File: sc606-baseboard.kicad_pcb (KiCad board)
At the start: 2 copper layers, 100 x 90 mm, 398 parts, among them IC1 TPS54561DPRT, IC2 TPS7A0518PDBVT, J1 PJ-202A, J10 WE_632723300011, J11 WE_632723300011, J12 U_FL-R-SMT-1_10_, J2 WE_68715014522, J3 F52R-1A7H1-11020, J4 46756-1001, J5 U_FL-R-SMT-1_10_, J6 U_FL-R-SMT-1_10_, J7 DM3AT-SF-PEJM5, J8 693022010811, J9 0473460001, M1 SC606T, Q1 BSS138APW, Q2 BSS138-7-F, Q3 BSS138APW, Q4 BSS138APW, Q5 BSS138APW, Q6 BSS138APW, Q7 BSS138-7-F, Q8 BSS138-7-F, SW1 1X03, U1 AP62301WU-7, U10 NCP163ASN330T1G, U11 EMIF06-MSD02N16, U12 FSUSB30MUX, U13 FT232RQ-REEL, U15 USB57442G, U2 AP62301WU-7, U3 AP62301WU-7, U4 74LVC1G123GN, U5 NTS0102GT, U6 PCA9547BS, U7 LT9611UXC, U8 NTS0102GT, U9 TPD13S523PWR, Y1 ABM8G-24.000MHZ-18-D2Y-T, Y2 ABM8G-25.000MHZ-B4Y-T

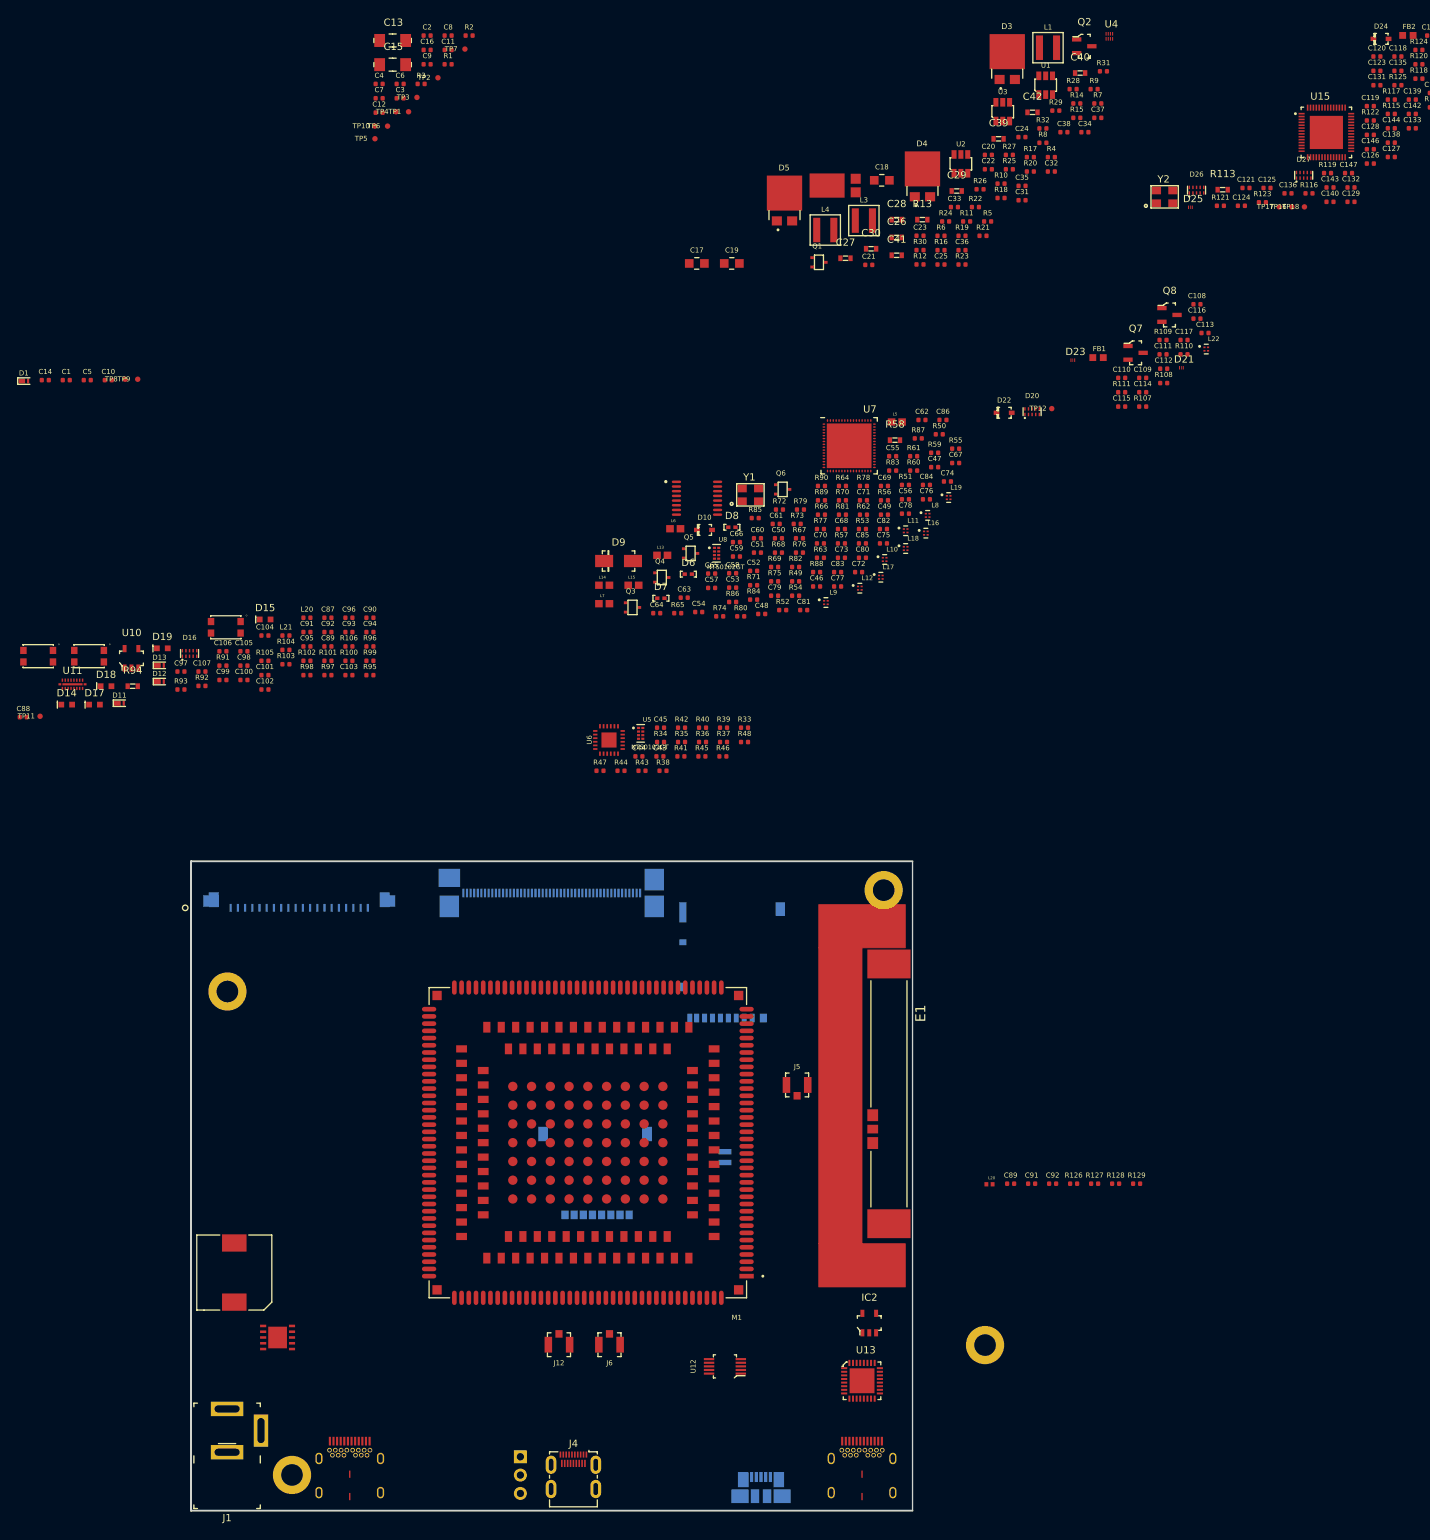
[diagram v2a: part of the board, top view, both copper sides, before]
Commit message: Main components placed on board
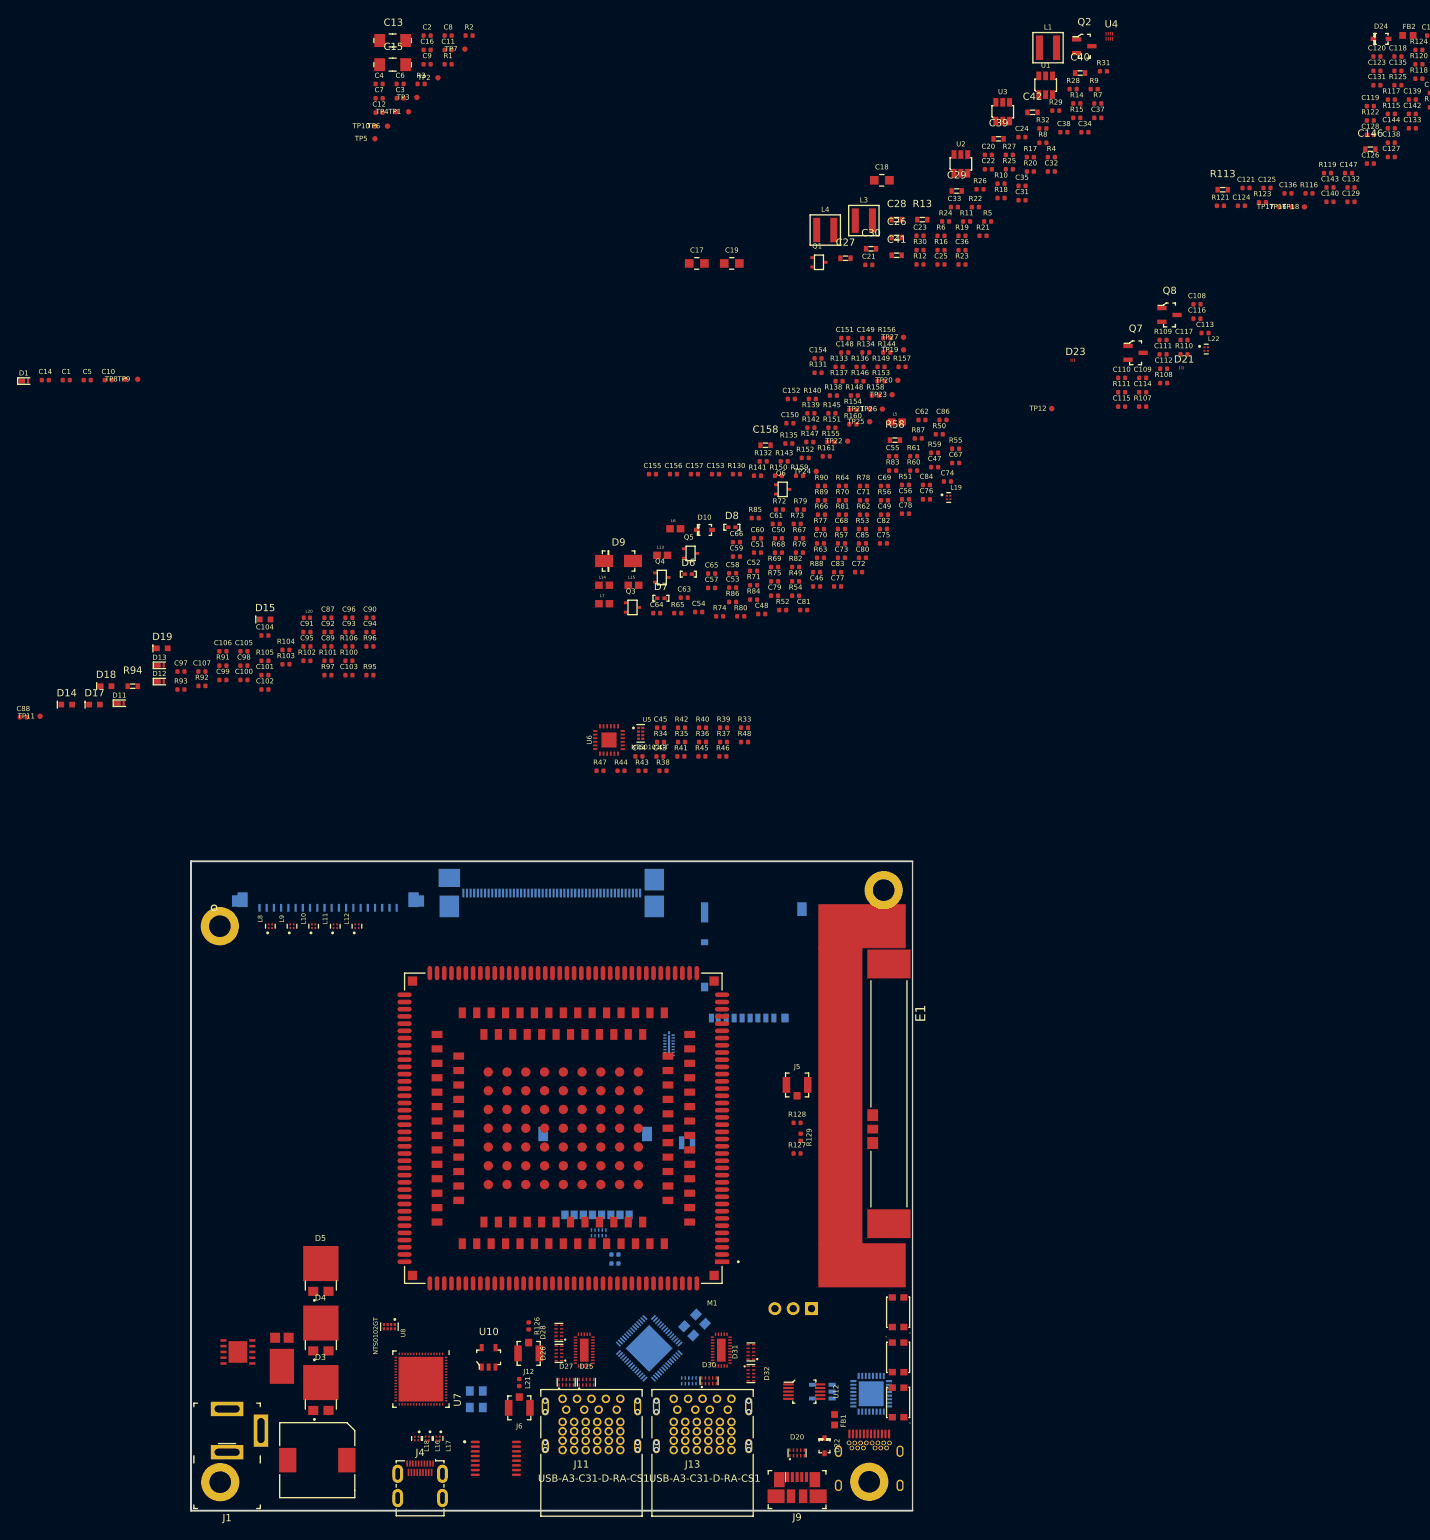
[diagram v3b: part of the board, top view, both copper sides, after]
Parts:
- removed the C89 at (188.6, 84.7)
- removed the C91 at (191.5, 84.7)
- removed the C92 at (194.4, 84.7)
- removed the L20 at (185.7, 84.8)
- added C148: C_100n_0402, sc606-baseboard-footprints:0402-cap, F.Cu at (165.6, -30.5)
- added C149: C_100n_0402, sc606-baseboard-footprints:0402-cap, F.Cu at (168.5, -32.5)
- added C150: C_100n_0402, sc606-baseboard-footprints:0402-cap, F.Cu at (158.0, -20.7)
- added C151: C_100n_0402, sc606-baseboard-footprints:0402-cap, F.Cu at (165.6, -32.5)
- added C152: C_10u_0402, sc606-baseboard-footprints:0402-cap, F.Cu at (158.2, -24.1)
- added C153: C_100n_0402, sc606-baseboard-footprints:0402-cap, F.Cu at (147.7, -13.7)
- added C154: C_100n_0402, sc606-baseboard-footprints:0402-cap, F.Cu at (161.9, -29.7)
- added C155: C_100n_0402, sc606-baseboard-footprints:0402-cap, F.Cu at (139.0, -13.7)
- added C156: C_100n_0402, sc606-baseboard-footprints:0402-cap, F.Cu at (141.9, -13.7)
- added C157: C_100n_0402, sc606-baseboard-footprints:0402-cap, F.Cu at (144.8, -13.7)
- added C158: C_47u_0603, antmicro-footprints:0603-cap, F.Cu at (154.6, -17.7)
- added D28: PUSB3F96X_PASS, sc606-baseboard-footprints:PUSB3F96X, F.Cu at (126.0, 105.3)
- added D29: PUSB3F96X_PASS, sc606-baseboard-footprints:PUSB3F96X, B.Cu at (144.0, 112.0)
- added D30: PUSB3F96X_PASS, sc606-baseboard-footprints:PUSB3F96X, F.Cu at (146.8, 112.0)
- added D31: PUSB3F96X_PASS, sc606-baseboard-footprints:PUSB3F96X, F.Cu at (152.6, 108.0)
- added D32: PUSB3F96X_PASS, sc606-baseboard-footprints:PUSB3F96X, F.Cu at (152.6, 111.0)
- added IC3: HD3SS3220, antmicro-footprints:RNH0030A, F.Cu at (129.5, 107.8)
- added IC4: HD3SS3220, antmicro-footprints:RNH0030A, F.Cu at (148.5, 107.8)
- added J13: USB-A3-C31-D-RA-CS1, antmicro-footprints:USB-A3-C31-D-RA-CS1, F.Cu at (142.4, 116.0)
- added R130: R_200k_0402, antmicro-footprints:0402-res, F.Cu at (150.6, -13.7)
- added R131: R_10k_0402, antmicro-footprints:0402-res, F.Cu at (161.9, -27.7)
- added R132: R_2k_0402, antmicro-footprints:0402-res, F.Cu at (154.3, -15.4)
- added R133: R_0R_0402, antmicro-footprints:0402-res, F.Cu at (164.8, -28.5)
- added R134: R_0R_0402, antmicro-footprints:0402-res, F.Cu at (168.5, -30.5)
- added R135: R_0R_0402, antmicro-footprints:0402-res, F.Cu at (157.9, -17.9)
- added R136: R_0R_0402, antmicro-footprints:0402-res, F.Cu at (167.7, -28.5)
- added R137: R_0R_0402, antmicro-footprints:0402-res, F.Cu at (164.8, -26.5)
- added R138: R_0R_0402, antmicro-footprints:0402-res, F.Cu at (164.0, -24.5)
- added R139: R_2k_0402, antmicro-footprints:0402-res, F.Cu at (160.9, -22.1)
- added R140: R_2k_0402, antmicro-footprints:0402-res, F.Cu at (161.1, -24.1)
- added R141: R_909k_0402, antmicro-footprints:0402-res, F.Cu at (153.5, -13.4)
- added R142: R_200k_0402, antmicro-footprints:0402-res, F.Cu at (160.9, -20.1)
- added R143: R_0R_0402, antmicro-footprints:0402-res, F.Cu at (157.2, -15.4)
- added R144: R_200k_0402, antmicro-footprints:0402-res, F.Cu at (171.4, -30.5)
- added R145: R_10k_0402, antmicro-footprints:0402-res, F.Cu at (163.8, -22.1)
- added R146: R_2k_0402, antmicro-footprints:0402-res, F.Cu at (167.7, -26.5)
- added R147: R_0R_0402, antmicro-footprints:0402-res, F.Cu at (160.8, -18.1)
- added R148: R_0R_0402, antmicro-footprints:0402-res, F.Cu at (166.9, -24.5)
- added R149: R_0R_0402, antmicro-footprints:0402-res, F.Cu at (170.6, -28.5)
- added R150: R_0R_0402, antmicro-footprints:0402-res, F.Cu at (156.4, -13.4)
- added R151: R_0R_0402, antmicro-footprints:0402-res, F.Cu at (163.8, -20.1)
- added R152: R_0R_0402, antmicro-footprints:0402-res, F.Cu at (160.1, -15.9)
- added R153: R_2k_0402, antmicro-footprints:0402-res, F.Cu at (170.6, -26.5)
- added R154: R_2k_0402, antmicro-footprints:0402-res, F.Cu at (166.7, -22.6)
- added R155: R_0R_0402, sc606-baseboard-footprints:0402-res, F.Cu at (163.7, -18.1)
- added R156: R_0R_0402, sc606-baseboard-footprints:0402-res, F.Cu at (171.4, -32.5)
- added R157: R_0R_0402, sc606-baseboard-footprints:0402-res, F.Cu at (173.5, -28.5)
- added R158: R_0R_0402, sc606-baseboard-footprints:0402-res, F.Cu at (169.8, -24.5)
- added R159: R_909k_0402, antmicro-footprints:0402-res, F.Cu at (159.3, -13.4)
- added R160: R_200k_0402, antmicro-footprints:0402-res, F.Cu at (166.7, -20.6)
- added R161: R_0R_0402, antmicro-footprints:0402-res, F.Cu at (163.0, -16.1)
- added TP19: TP_SMD_0_75MM, sc606-baseboard-footprints:Testpoint_smd_0_75mm, F.Cu at (173.8, -30.8)
- added TP20: TP_SMD_0_75MM, sc606-baseboard-footprints:Testpoint_smd_0_75mm, F.Cu at (173.0, -26.6)
- added TP21: TP_SMD_0_75MM, sc606-baseboard-footprints:Testpoint_smd_0_75mm, F.Cu at (169.1, -22.6)
- added TP22: TP_SMD_0_75MM, sc606-baseboard-footprints:Testpoint_smd_0_75mm, F.Cu at (166.0, -18.2)
- added TP23: TP_SMD_0_75MM, sc606-baseboard-footprints:Testpoint_smd_0_75mm, F.Cu at (172.2, -24.6)
- added TP24: TP_SMD_0_75MM, sc606-baseboard-footprints:Testpoint_smd_0_75mm, F.Cu at (161.7, -14.0)
- added TP25: TP_SMD_0_75MM, sc606-baseboard-footprints:Testpoint_smd_0_75mm, F.Cu at (169.1, -20.9)
- added TP26: TP_SMD_0_75MM, sc606-baseboard-footprints:Testpoint_smd_0_75mm, F.Cu at (170.8, -22.6)
- added TP27: TP_SMD_0_75MM, sc606-baseboard-footprints:Testpoint_smd_0_75mm, F.Cu at (173.8, -32.6)
- C102, C103: value C_0p5_0402 -> C_100n_0402
- C139: value C_100n_0402 -> C_10u_0402
- C146: value C_10u_0402 -> C_47u_0603; footprint sc606-baseboard-footprints:0402-cap -> antmicro-footprints:0603-cap
- C89, C91: value C_0p5_0402 -> C_1u_0402
- C92: value C_6p9_0402 -> C_3p_0402
- C94: value C_0p9_0402 -> C_100n_0402
- D16, IC2, R98, R99, U11, U13, U15, Y1, Y2: moved to B.Cu
- D25: value PESD5V0C2BDFZ -> PUSB3F96X_PASS; footprint sc606-baseboard-footprints:DFN0603-3 -> sc606-baseboard-footprints:PUSB3F96X
- J11: value WE_632723300011 -> USB-A3-C31-D-RA-CS1; footprint sc606-baseboard-footprints:WE_632723300011 -> antmicro-footprints:USB-A3-C31-D-RA-CS1
- J9: moved to F.Cu
- L20: value LQW15AN2N4B00D -> HK10056N8S-T; footprint sc606-baseboard-footprints:0402-res -> sc606-baseboard-footprints:INDC1005X55N
- moved D3 207.5 mm to (93.0, 113.2)
- moved D27 196.0 mm to (127.0, 112.2)
- moved U15 192.9 mm to (138.5, 107.5), turned to 135 degrees
- moved D26 183.8 mm to (126.0, 108.2), turned to 90 degrees
- moved D25 183.1 mm to (129.8, 112.2)
- moved D4 180.4 mm to (93.0, 105.0)
- moved D2 180.1 mm to (87.5, 109.5), turned to 90 degrees
- moved Y2 169.3 mm to (144.8, 104.2), turned to 225 degrees
- moved D5 161.7 mm to (93.0, 96.8)
- moved S1 153.8 mm to (173.0, 108.8), turned to 90 degrees
- moved FB1 151.7 mm to (164.2, 117.4), turned to 270 degrees
- moved D20 147.9 mm to (159.0, 122.0)
- moved D22 145.3 mm to (162.8, 121.0), turned to 270 degrees
- moved S3 144.4 mm to (173.0, 102.5), turned to 270 degrees
- moved L16 143.2 mm to (107.8, 120.0), turned to 270 degrees
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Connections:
- C102 pad 1: Net-(ANT2-Pad7) -> Net-(C102-Pad1)
- C102 pad 2: GND -> /USB_HUB_Connectors/USB_C1_SS_TX2_N
- C103 pad 1: Net-(ANT2-Pad6) -> GND
- C103 pad 2: GND -> /USB_HUB_Connectors/5V0_USB
- C138 pad 2: /USB_HUB_Connectors/USBSS_TX1_P -> /USB_HUB_Connectors/USB_C1_SS_TX1_P
- C139 pad 1: Net-(C139-Pad1) -> /USB_HUB_Connectors/5V0_USB
- C139 pad 2: /USB_HUB_Connectors/USBSS_RX2_N -> GND
- C140 pad 2: /USB_HUB_Connectors/USBSS_RX2_P -> /USB_HUB_Connectors/USB_C1_SS_RX2_N
- C141 pad 2: /USB_HUB_Connectors/USBSS_TX1_N -> /USB_HUB_Connectors/USB_C1_SS_TX1_N
- C142 pad 1: /USB_HUB_Connectors/USBSS_RX1_P -> Net-(C142-Pad1)
- C142 pad 2: Net-(C142-Pad2) -> /USB_HUB_Connectors/USB_C1_SS_RX1_N
- C143 pad 1: /USB_HUB_Connectors/USBSS_TX2_N -> Net-(C143-Pad1)
- C143 pad 2: Net-(C143-Pad2) -> /USB_HUB_Connectors/USB_C1_SS_RX2_P
- C144 pad 1: GND -> Net-(C144-Pad1)
- C144 pad 2: /USB_HUB_Connectors/5V0_USB -> /USB_HUB_Connectors/USB_C1_SS_RX1_P
- C145 pad 1: /USB_HUB_Connectors/USBSS_RX1_N -> GND
- C145 pad 2: Net-(C145-Pad2) -> 3V3_SYS
- C146 pad 1: /USB_HUB_Connectors/5V0_USB -> 5V0_SYS
- C147 pad 1: /USB_HUB_Connectors/USBSS_TX2_P -> Net-(C147-Pad1)
- C147 pad 2: Net-(C147-Pad2) -> /USB_HUB_Connectors/USB_C2_SS_TX1_P
- C89 pad 1: ANT_MAIN -> ANT-WIFI
- C92 pad 1: Net-(ANT2-Pad4) -> Net-(C92-Pad1)
- C92 pad 2: Net-(C91-Pad1) -> ANT_MAIN
- C94 pad 1: Net-(ANT2-Pad4) -> Net-(C94-Pad1)
- C94 pad 2: GND -> /USB_HUB_Connectors/USB_C1_SS_TX2_P
- D25 pad 1: /USB_HUB_Connectors/USB_D_P -> /USB_HUB_Connectors/USB_A1_SS_TX_P
- D25 pad 2: /USB_HUB_Connectors/USB_D_N -> /USB_HUB_Connectors/USB_A1_SS_TX_N
- D26 pad 1: /USB_HUB_Connectors/USBSS_TX2_P -> /USB_HUB_Connectors/USB_C1_D_P
- D26 pad 10: /USB_HUB_Connectors/USBSS_TX2_P -> /USB_HUB_Connectors/USB_C1_D_P
- D26 pad 2: /USB_HUB_Connectors/USBSS_TX2_N -> /USB_HUB_Connectors/USB_C1_D_N
- D26 pad 4: /USB_HUB_Connectors/USBSS_RX2_N -> /USB_HUB_Connectors/USB_A1_D_N
- D26 pad 5: /USB_HUB_Connectors/USBSS_RX2_P -> /USB_HUB_Connectors/USB_A1_D_P
- D26 pad 6: /USB_HUB_Connectors/USBSS_RX2_P -> /USB_HUB_Connectors/USB_A1_D_P
- D26 pad 7: /USB_HUB_Connectors/USBSS_RX2_N -> /USB_HUB_Connectors/USB_A1_D_N
- D26 pad 9: /USB_HUB_Connectors/USBSS_TX2_N -> /USB_HUB_Connectors/USB_C1_D_N
- D27 pad 1: /USB_HUB_Connectors/USBSS_TX1_P -> /USB_HUB_Connectors/USB_C1_SS_RX2_P
- D27 pad 10: /USB_HUB_Connectors/USBSS_TX1_P -> /USB_HUB_Connectors/USB_C1_SS_RX2_P
- D27 pad 2: /USB_HUB_Connectors/USBSS_TX1_N -> /USB_HUB_Connectors/USB_C1_SS_RX2_N
- D27 pad 4: /USB_HUB_Connectors/USBSS_RX1_N -> /USB_HUB_Connectors/USB_C1_SS_TX2_P
- D27 pad 5: /USB_HUB_Connectors/USBSS_RX1_P -> /USB_HUB_Connectors/USB_C1_SS_TX2_N
- D27 pad 6: /USB_HUB_Connectors/USBSS_RX1_P -> /USB_HUB_Connectors/USB_C1_SS_TX2_N
- D27 pad 7: /USB_HUB_Connectors/USBSS_RX1_N -> /USB_HUB_Connectors/USB_C1_SS_TX2_P
- D27 pad 9: /USB_HUB_Connectors/USBSS_TX1_N -> /USB_HUB_Connectors/USB_C1_SS_RX2_N
- J11 pad A10: Net-(C139-Pad1) -> Net-(C140-Pad1)
- J11 pad A11: Net-(C140-Pad1) -> Net-(C143-Pad1)
- J11 pad A6: /USB_HUB_Connectors/USB_1_D_P -> /USB_HUB_Connectors/USB_C1_D_P
- J11 pad A7: /USB_HUB_Connectors/USB_1_D_N -> /USB_HUB_Connectors/USB_C1_D_N
- J11 pad B10: Net-(C145-Pad2) -> Net-(C142-Pad1)
- J11 pad B11: Net-(C142-Pad2) -> Net-(C144-Pad1)
- J11 pad B2: Net-(C147-Pad2) -> Net-(C94-Pad1)
- J11 pad B3: Net-(C143-Pad2) -> Net-(C102-Pad1)
- J11 pad B6: /USB_HUB_Connectors/USB_1_D_P -> /USB_HUB_Connectors/USB_C1_D_P
- J11 pad B7: /USB_HUB_Connectors/USB_1_D_N -> /USB_HUB_Connectors/USB_C1_D_N
- J2 pad 1: /cameras module/CSI0_LN3_N -> CAM1_DATA_7
- J2 pad 10: /cameras module/CSI0_CLK_N -> CAM1_DATA_9
- J2 pad 11: /cameras module/CSI0_CLK_P -> CAM1_DATA_8
- J2 pad 19: /cameras module/CSI1_LN3_N -> CAM2_DATA_7
- J2 pad 2: /cameras module/CSI0_LN3_P -> CAM1_DATA_6
- J2 pad 20: /cameras module/CSI1_LN3_P -> CAM2_DATA_6
- J2 pad 21: /cameras module/CSI1_LN2_N -> CAM2_DATA_5
- J2 pad 22: /cameras module/CSI1_LN2_P -> CAM2_DATA_4
- J2 pad 23: /cameras module/CSI1_LN1_N -> CAM2_DATA_3
- J2 pad 24: /cameras module/CSI1_LN1_P -> CAM2_DATA_2
- J2 pad 25: /cameras module/CSI1_LN0_N -> CAM2_DATA_1
- J2 pad 26: /cameras module/CSI1_LN0_P -> CAM2_DATA_0
- J2 pad 28: /cameras module/CSI1_CLK_N -> CAM2_DATA_9
- J2 pad 29: /cameras module/CSI1_CLK_P -> CAM2_DATA_8
- J2 pad 3: /cameras module/CSI0_LN2_N -> CAM1_DATA_5
- J2 pad 4: /cameras module/CSI0_LN2_P -> CAM1_DATA_4
- J2 pad 5: /cameras module/CSI0_LN1_N -> CAM1_DATA_3
- J2 pad 6: /cameras module/CSI0_LN1_P -> CAM1_DATA_2
- J2 pad 7: /cameras module/CSI0_LN0_N -> CAM1_DATA_1
- J2 pad 8: /cameras module/CSI0_LN0_P -> CAM1_DATA_0
- J7 pad 10: /peripherals/SD_DET -> SD_DATA_6
- L10 pad 1: /display module/DSI0_LN1_N -> SoMtoDisplay_DATA_3
- L10 pad 4: /display module/DSI0_LN1_P -> SoMtoDisplay_DATA_2
- L11 pad 1: /display module/DSI0_LN0_N -> SoMtoDisplay_DATA_1
- L11 pad 4: /display module/DSI0_LN0_P -> SoMtoDisplay_DATA_0
- L12 pad 1: /display module/DSI0_CLK_N -> SoMtoDisplay_DATA_9
- L12 pad 4: /display module/DSI0_CLK_P -> SoMtoDisplay_DATA_8
- L20 pad 1: ANT_MAIN -> Net-(C92-Pad1)
- L20 pad 2: Net-(C91-Pad1) -> GND
- L8 pad 1: /display module/DSI0_LN3_N -> SoMtoDisplay_DATA_7
- L8 pad 4: /display module/DSI0_LN3_P -> SoMtoDisplay_DATA_6
- L9 pad 1: /display module/DSI0_LN2_N -> SoMtoDisplay_DATA_5
- L9 pad 4: /display module/DSI0_LN2_P -> SoMtoDisplay_DATA_4
- M1 pad 102: /SoM/DSI1_CLK_P -> SoMtoDisplay_DATA_8
- M1 pad 103: /SoM/DSI1_CLK_N -> SoMtoDisplay_DATA_9
- M1 pad 104: /SoM/DSI1_LN0_P -> SoMtoDisplay_DATA_0
- M1 pad 105: /SoM/DSI1_LN0_N -> SoMtoDisplay_DATA_1
- M1 pad 106: /SoM/DSI1_LN1_P -> SoMtoDisplay_DATA_2
- M1 pad 107: /SoM/DSI1_LN1_N -> SoMtoDisplay_DATA_3
- M1 pad 108: /SoM/DSI1_LN2_P -> SoMtoDisplay_DATA_4
- M1 pad 109: /SoM/DSI1_LN2_N -> SoMtoDisplay_DATA_5
- M1 pad 110: /SoM/DSI1_LN3_P -> SoMtoDisplay_DATA_6
- M1 pad 111: /SoM/DSI1_LN3_N -> SoMtoDisplay_DATA_7
- M1 pad 115: /SoM/DSI0_CLK_P -> SoMtoHDMI_DATA_8
- M1 pad 116: /SoM/DSI0_CLK_N -> SoMtoHDMI_DATA_9
- M1 pad 117: /SoM/DSI0_LN0_P -> SoMtoHDMI_DATA_0
- M1 pad 118: /SoM/DSI0_LN0_N -> SoMtoHDMI_DATA_1
- M1 pad 119: /SoM/DSI0_LN1_P -> SoMtoHDMI_DATA_2
- M1 pad 120: /SoM/DSI0_LN1_N -> SoMtoHDMI_DATA_3
- M1 pad 121: /SoM/DSI0_LN2_P -> SoMtoHDMI_DATA_4
- M1 pad 122: /SoM/DSI0_LN2_N -> SoMtoHDMI_DATA_5
- M1 pad 123: /SoM/DSI0_LN3_P -> SoMtoHDMI_DATA_6
- M1 pad 124: /SoM/DSI0_LN3_N -> SoMtoHDMI_DATA_7
- M1 pad 183: /SoM/CSI1_CLK_P -> CAM2_DATA_8
- M1 pad 184: /SoM/CSI1_CLK_N -> CAM2_DATA_9
- M1 pad 185: /SoM/CSI1_LN0_P -> CAM2_DATA_0
- M1 pad 186: /SoM/CSI1_LN0_N -> CAM2_DATA_1
- M1 pad 187: /SoM/CSI1_LN1_P -> CAM2_DATA_2
- M1 pad 188: /SoM/CSI1_LN1_N -> CAM2_DATA_3
- M1 pad 189: /SoM/CSI1_LN2_P -> CAM2_DATA_4
- M1 pad 190: /SoM/CSI1_LN2_N -> CAM2_DATA_5
- M1 pad 191: /SoM/CSI1_LN3_P -> CAM2_DATA_6
- M1 pad 192: /SoM/CSI1_LN3_N -> CAM2_DATA_7
- M1 pad 64: /SoM/SD_DET -> SD_DATA_6
- M1 pad 65: /SoM/SD_DATA3 -> SD_DATA_3
- M1 pad 66: /SoM/SD_DATA2 -> SD_DATA_2
- M1 pad 67: /SoM/SD_DATA1 -> SD_DATA_1
- M1 pad 68: /SoM/SD_DATA0 -> SD_DATA_0
- M1 pad 69: /SoM/SD_CMD -> SD_DATA_5
- M1 pad 70: /SoM/SD_CLK -> SD_DATA_4
- M1 pad 88: /SoM/CSI0_CLK_P -> CAM1_DATA_8
- M1 pad 89: /SoM/CSI0_CLK_N -> CAM1_DATA_9
- M1 pad 90: /SoM/CSI0_LN0_P -> CAM1_DATA_0
- M1 pad 91: /SoM/CSI0_LN0_N -> CAM1_DATA_1
- M1 pad 92: /SoM/CSI0_LN1_P -> CAM1_DATA_2
- M1 pad 93: /SoM/CSI0_LN1_N -> CAM1_DATA_3
- M1 pad 94: /SoM/CSI0_LN2_P -> CAM1_DATA_4
- M1 pad 95: /SoM/CSI0_LN2_N -> CAM1_DATA_5
- M1 pad 96: /SoM/CSI0_LN3_P -> CAM1_DATA_6
- M1 pad 97: /SoM/CSI0_LN3_N -> CAM1_DATA_7
- R122 pad 1: /USB_HUB_Connectors/CC2 -> /USB_HUB_Connectors/USB_C1_CC1
- R122 pad 2: Net-(J11-PadA5) -> Net-(J11-PadB5)
- R123 pad 1: /USB_HUB_Connectors/CC1 -> /USB_HUB_Connectors/USB_C1_CC2
- R123 pad 2: Net-(J11-PadA5) -> Net-(J11-PadB5)
- R124 pad 1: /USB_HUB_Connectors/CC2 -> /USB_HUB_Connectors/USB_C1_CC2
- R124 pad 2: Net-(J11-PadB5) -> Net-(J11-PadA5)
- R125 pad 1: /USB_HUB_Connectors/CC1 -> /USB_HUB_Connectors/USB_C1_CC1
- R125 pad 2: Net-(J11-PadB5) -> Net-(J11-PadA5)
- TP18 pad 1: Net-(J11-PadB8) -> Net-(J11-PadA8)
- U11 pad 1: /peripherals/SD_DET -> SD_DATA_6
- U11 pad 3: /peripherals/SD_DATA2 -> SD_DATA_2
- U11 pad 4: /peripherals/SD_DATA3 -> SD_DATA_3
- U11 pad 5: /peripherals/SD_CMD -> SD_DATA_5
- U11 pad 6: /peripherals/SD_CLK -> SD_DATA_4
- U11 pad 7: /peripherals/SD_DATA0 -> SD_DATA_0
- U11 pad 8: /peripherals/SD_DATA1 -> SD_DATA_1
- U15 pad 1: /USB_HUB_Connectors/USB_1_D_P -> /USB_HUB_Connectors/USB_A1_D_P
- U15 pad 10: Net-(U15-Pad10) -> /USB_HUB_Connectors/USB_C1_SS_TX_P
- U15 pad 11: Net-(U15-Pad11) -> /USB_HUB_Connectors/USB_C1_SS_TX_N
- U15 pad 13: Net-(U15-Pad13) -> /USB_HUB_Connectors/USB_C1_SS_RX_P
- U15 pad 14: Net-(U15-Pad14) -> /USB_HUB_Connectors/USB_C1_SS_RX_N
- U15 pad 17: Net-(U15-Pad17) -> /USB_HUB_Connectors/USB_A2_D_P
- U15 pad 18: Net-(U15-Pad18) -> /USB_HUB_Connectors/USB_A2_D_N
- U15 pad 19: Net-(U15-Pad19) -> /USB_HUB_Connectors/USB_A2_SS_TX_P
- U15 pad 2: /USB_HUB_Connectors/USB_1_D_N -> /USB_HUB_Connectors/USB_A1_D_N
- U15 pad 20: Net-(U15-Pad20) -> /USB_HUB_Connectors/USB_A2_SS_TX_N
- U15 pad 22: Net-(U15-Pad22) -> /USB_HUB_Connectors/USB_A2_SS_RX_P
- U15 pad 23: Net-(U15-Pad23) -> /USB_HUB_Connectors/USB_A2_SS_RX_N
- U15 pad 24: Net-(U15-Pad24) -> /USB_HUB_Connectors/USB_C2_D_P
- U15 pad 25: Net-(U15-Pad25) -> /USB_HUB_Connectors/USB_C2_D_N
- U15 pad 26: Net-(U15-Pad26) -> /USB_HUB_Connectors/USB_C2_SS_TX_P
- U15 pad 27: Net-(U15-Pad27) -> /USB_HUB_Connectors/USB_C2_SS_TX_N
- U15 pad 29: Net-(U15-Pad29) -> /USB_HUB_Connectors/USB_C2_SS_RX_P
- U15 pad 3: /USB_HUB_Connectors/USBSS_TX1_P -> /USB_HUB_Connectors/USB_A1_SS_TX_P
- U15 pad 30: Net-(U15-Pad30) -> /USB_HUB_Connectors/USB_C2_SS_RX_N
- U15 pad 4: /USB_HUB_Connectors/USBSS_TX1_N -> /USB_HUB_Connectors/USB_A1_SS_TX_N
- U15 pad 47: SoM_USB3_TX_P -> SoM_USB3_RX_P
- U15 pad 48: SoM_USB3_TX_N -> SoM_USB3_RX_N
- U15 pad 50: SoM_USB3_RX_P -> SoM_USB3_TX_P
- U15 pad 51: SoM_USB3_RX_N -> SoM_USB3_TX_N
- U15 pad 6: /USB_HUB_Connectors/USBSS_RX1_P -> /USB_HUB_Connectors/USB_A1_SS_RX_P
- U15 pad 7: /USB_HUB_Connectors/USBSS_RX1_N -> /USB_HUB_Connectors/USB_A1_SS_RX_N
- U15 pad 8: Net-(U15-Pad8) -> /USB_HUB_Connectors/USB_C1_D_P
- U15 pad 9: Net-(U15-Pad9) -> /USB_HUB_Connectors/USB_C1_D_N
- U7 pad 10: /display module/DSI1_CLK_P -> SoMtoHDMI_DATA_8
- U7 pad 11: /display module/DSI1_LN1_N -> SoMtoHDMI_DATA_3
- U7 pad 12: /display module/DSI1_LN1_P -> SoMtoHDMI_DATA_2
- U7 pad 13: /display module/DSI1_LN0_N -> SoMtoHDMI_DATA_1
- U7 pad 14: /display module/DSI1_LN0_P -> SoMtoHDMI_DATA_0
- U7 pad 5: /display module/DSI1_LN3_N -> SoMtoHDMI_DATA_7
- U7 pad 6: /display module/DSI1_LN3_P -> SoMtoHDMI_DATA_6
- U7 pad 7: /display module/DSI1_LN2_N -> SoMtoHDMI_DATA_5
- U7 pad 8: /display module/DSI1_LN2_P -> SoMtoHDMI_DATA_4
- U7 pad 9: /display module/DSI1_CLK_N -> SoMtoHDMI_DATA_9

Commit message: Main 5V buck converter placed and routed
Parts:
- moved TP27 231.5 mm to (103.7, 188.1), turned to 180 degrees
- moved R156 230.0 mm to (106.1, 188.0), turned to 180 degrees
- moved C149 228.4 mm to (109.0, 188.0), turned to 180 degrees
- moved TP19 228.2 mm to (103.7, 186.3), turned to 180 degrees
- moved C151 227.0 mm to (111.9, 188.0), turned to 180 degrees
- moved R144 226.2 mm to (106.1, 186.0), turned to 180 degrees
- moved R134 224.6 mm to (109.0, 186.0), turned to 180 degrees
- moved R157 223.7 mm to (104.0, 184.0), turned to 180 degrees
- moved C148 223.1 mm to (111.9, 186.0), turned to 180 degrees
- moved R149 221.9 mm to (106.9, 184.0), turned to 180 degrees
- moved C118 221.4 mm to (176.8, 140.0)
- moved C119 221.4 mm to (172.9, 146.8)
- moved C120 221.4 mm to (173.9, 140.0)
- moved C121 221.4 mm to (155.7, 158.2)
- moved C122 221.4 mm to (182.6, 139.1)
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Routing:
- net GND: track 0.00 -> 36.2 mm, vias 0 -> 6
- net Net-(C25-Pad2): track 0.00 -> 17.2 mm
- net 5V0_SYS: track 0.00 -> 15.2 mm, vias 0 -> 11
- net Net-(IC1-Pad6): track 0.00 -> 8.35 mm, vias 0 -> 2
- net Net-(D4-Pad3): track 0.00 -> 6.95 mm
- net Net-(D3-Pad3): track 0.00 -> 6.95 mm
- net Net-(C23-Pad1): track 0.00 -> 6.44 mm
- net Net-(IC1-Pad10): track 0.00 -> 4.80 mm, vias 0 -> 2
- net Net-(C25-Pad1): track 0.00 -> 4.30 mm
- net Net-(IC1-Pad3): track 0.00 -> 3.73 mm
- net Net-(C20-Pad1): track 0.00 -> 2.64 mm
- net Net-(IC1-Pad5): track 0.00 -> 2.56 mm
- net Net-(R13-Pad2): track 0.00 -> 1.90 mm
- net Net-(C22-Pad1): track 0.00 -> 1.02 mm
- added copper zone on F.Cu, net 5V0_SYS
- added copper zone on In3.5V0, net 5V0_SYS
- added copper zone on In1.GND, net GND
- added copper zone on F.Cu, net Net-(D3-Pad3)
- added copper zone on F.Cu, net Net-(D4-Pad3)
- added copper zone on F.Cu, net VCC
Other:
- copper layers 2 -> 6
